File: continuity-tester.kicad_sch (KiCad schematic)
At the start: 30 parts, among them J1 Conn_01x01_Pin, J2 Conn_01x01_Pin, J3 Conn_01x01_Pin, J4 Conn_01x01_Pin, Q1 2N3906, Q2 2N3904, Q3 2N3904, U1 MCP6022

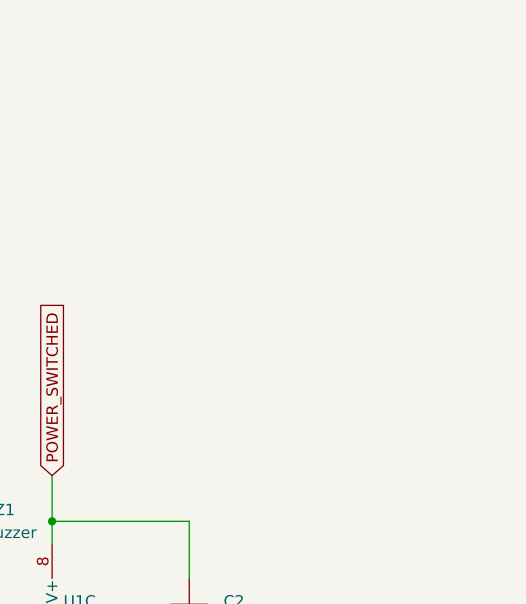
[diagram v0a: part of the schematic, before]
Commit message: added board dimensions to silkscreen
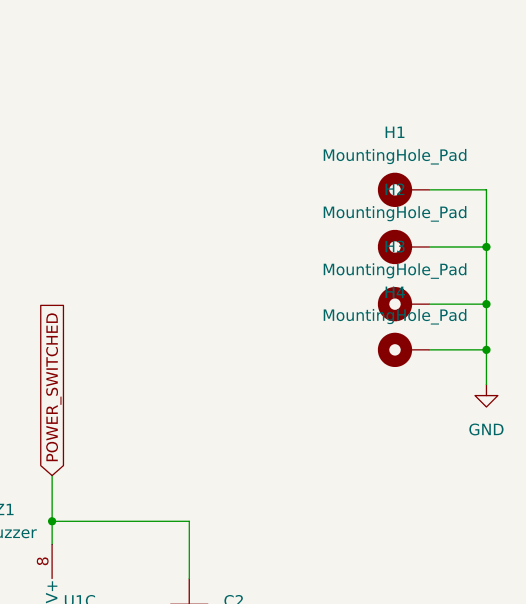
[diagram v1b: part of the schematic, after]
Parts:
- added H1, H2, H3, H4: MountingHole_Pad, MountingHole:MountingHole_2mm, symbol Mechanical:MountingHole_Pad
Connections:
- net GND: now also H1.1, H2.1, H3.1, H4.1
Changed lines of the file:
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@@
 (kicad_sch (version 20230121) (generator eeschema)
   (paper "A4")
+  (junction (at 236.22 68.58) (diameter 0) (color 0 0 0 0)
+  )
   (junction (at 92.71 101.6) (diameter 0) (color 0 0 0 0)
   )
@@
   (junction (at 129.54 96.52) (diameter 0) (color 0 0 0 0)
   )
+  (junction (at 236.22 57.15) (diameter 0) (color 0 0 0 0)
+  )
   (junction (at 127 96.52) (diameter 0) (color 0 0 0 0)
   )
   (junction (at 88.9 91.44) (diameter 0) (color 0 0 0 0)
+  )
+  (junction (at 236.22 63.5) (diameter 0) (color 0 0 0 0)
   )
   (junction (at 50.8 63.5) (diameter 0) (color 0 0 0 0)
@@
     (stroke (width 0) (type default))
   )
+  (wire (pts (xy 229.87 57.15) (xy 236.22 57.15))
+    (stroke (width 0) (type default))
+  )
   (wire (pts (xy 88.9 86.36) (xy 88.9 91.44))
     (stroke (width 0) (type default))
   )
+  (wire (pts (xy 236.22 68.58) (xy 236.22 72.39))
+    (stroke (width 0) (type default))
+  )
   (wire (pts (xy 171.45 53.34) (xy 171.45 55.88))
     (stroke (width 0) (type default))
@@
     (stroke (width 0) (type default))
   )
+  (wire (pts (xy 236.22 63.5) (xy 236.22 68.58))
+    (stroke (width 0) (type default))
+  )
   (wire (pts (xy 173.99 85.09) (xy 170.18 85.09))
     (stroke (width 0) (type default))
@@
     (stroke (width 0) (type default))
   )
+  (wire (pts (xy 236.22 50.8) (xy 236.22 57.15))
+    (stroke (width 0) (type default))
+  )
   (wire (pts (xy 88.9 91.44) (xy 88.9 92.71))
     (stroke (width 0) (type default))
   )
+  (wire (pts (xy 229.87 68.58) (xy 236.22 68.58))
+    (stroke (width 0) (type default))
+  )
   (wire (pts (xy 40.64 109.22) (xy 40.64 113.03))
     (stroke (width 0) (type default))
@@
     (stroke (width 0) (type default))
   )
+  (wire (pts (xy 236.22 57.15) (xy 236.22 63.5))
+    (stroke (width 0) (type default))
+  )
+  (wire (pts (xy 229.87 50.8) (xy 236.22 50.8))
+    (stroke (width 0) (type default))
+  )
   (wire (pts (xy 187.96 82.55) (xy 187.96 87.63))
     (stroke (width 0) (type default))
@@
   )
   (wire (pts (xy 187.96 106.68) (xy 187.96 109.22))
+    (stroke (width 0) (type default))
+  )
+  (wire (pts (xy 229.87 63.5) (xy 236.22 63.5))
     (stroke (width 0) (type default))
   )
@@
     )
   )
+  (symbol (lib_id "Mechanical:MountingHole_Pad") (at 227.33 63.5 90) (unit 1)
+    (in_bom yes) (on_board yes) (dnp no) (fields_autoplaced)
+    (property "Reference" "H3" (at 226.06 57.15 90)
+      (effects (font (size 1.27 1.27)))
+    )
+    (property "Value" "MountingHole_Pad" (at 226.06 59.69 90)
+      (effects (font (size 1.27 1.27)))
+    )
+    (property "Footprint" "MountingHole:MountingHole_2mm" (at 227.33 63.5 0)
+      (effects (font (size 1.27 1.27)) hide)
+    )
+    (property "Datasheet" "~" (at 227.33 63.5 0)
+      (effects (font (size 1.27 1.27)) hide)
+    )
+    (pin "1")
+    (instances
+      (project "continuity-tester"
+        (path "/26eed4ac-2c8e-4cb2-b316-f57caaf9169f"
+          (reference "H3") (unit 1)
+        )
+      )
+    )
+  )
   (symbol (lib_id "power:GND") (at 88.9 92.71 0) (unit 1)
     (in_bom yes) (on_board yes) (dnp no) (fields_autoplaced)
@@
         (path "/26eed4ac-2c8e-4cb2-b316-f57caaf9169f"
           (reference "R3") (unit 1)
+        )
+      )
+    )
+  )
+  (symbol (lib_id "Mechanical:MountingHole_Pad") (at 227.33 50.8 90) (unit 1)
+    (in_bom yes) (on_board yes) (dnp no) (fields_autoplaced)
+    (property "Reference" "H1" (at 226.06 44.45 90)
+      (effects (font (size 1.27 1.27)))
+    )
+    (property "Value" "MountingHole_Pad" (at 226.06 46.99 90)
+      (effects (font (size 1.27 1.27)))
+    )
+    (property "Footprint" "MountingHole:MountingHole_2mm" (at 227.33 50.8 0)
+      (effects (font (size 1.27 1.27)) hide)
+    )
+    (property "Datasheet" "~" (at 227.33 50.8 0)
+      (effects (font (size 1.27 1.27)) hide)
+    )
+    (pin "1")
+    (instances
+      (project "continuity-tester"
+        (path "/26eed4ac-2c8e-4cb2-b316-f57caaf9169f"
+          (reference "H1") (unit 1)
         )
       )
@@
     )
   )
+  (symbol (lib_id "power:GND") (at 236.22 72.39 0) (unit 1)
+    (in_bom yes) (on_board yes) (dnp no) (fields_autoplaced)
+    (property "Reference" "#PWR014" (at 236.22 78.74 0)
+      (effects (font (size 1.27 1.27)) hide)
+    )
+    (property "Value" "GND" (at 236.22 77.47 0)
+      (effects (font (size 1.27 1.27)))
+    )
+    (property "Footprint" "" (at 236.22 72.39 0)
+      (effects (font (size 1.27 1.27)) hide)
+    )
+    (property "Datasheet" "" (at 236.22 72.39 0)
+      (effects (font (size 1.27 1.27)) hide)
+    )
+    (pin "1")
+    (instances
+      (project "continuity-tester"
+        (path "/26eed4ac-2c8e-4cb2-b316-f57caaf9169f"
+          (reference "#PWR014") (unit 1)
+        )
+      )
+    )
+  )
   (symbol (lib_id "Connector:Conn_01x01_Pin") (at 33.02 101.6 0) (unit 1)
     (in_bom yes) (on_board yes) (dnp no) (fields_autoplaced)
@@
     )
   )
+  (symbol (lib_id "Mechanical:MountingHole_Pad") (at 227.33 57.15 90) (unit 1)
+    (in_bom yes) (on_board yes) (dnp no) (fields_autoplaced)
+    (property "Reference" "H2" (at 226.06 50.8 90)
+      (effects (font (size 1.27 1.27)))
+    )
+    (property "Value" "MountingHole_Pad" (at 226.06 53.34 90)
+      (effects (font (size 1.27 1.27)))
+    )
+    (property "Footprint" "MountingHole:MountingHole_2mm" (at 227.33 57.15 0)
+      (effects (font (size 1.27 1.27)) hide)
+    )
+    (property "Datasheet" "~" (at 227.33 57.15 0)
+      (effects (font (size 1.27 1.27)) hide)
+    )
+    (pin "1")
+    (instances
+      (project "continuity-tester"
+        (path "/26eed4ac-2c8e-4cb2-b316-f57caaf9169f"
+          (reference "H2") (unit 1)
+        )
+      )
+    )
+  )
   (symbol (lib_id "power:GND") (at 40.64 113.03 0) (unit 1)
     (in_bom yes) (on_board yes) (dnp no) (fields_autoplaced)
@@
         )
       )
+    )
+  )
+  (symbol (lib_id "Mechanical:MountingHole_Pad") (at 227.33 68.58 90) (unit 1)
+    (in_bom yes) (on_board yes) (dnp no) (fields_autoplaced)
+    (property "Reference" "H4" (at 226.06 62.23 90)
+      (effects (font (size 1.27 1.27)))
+    )
+    (property "Value" "MountingHole_Pad" (at 226.06 64.77 90)
+      (effects (font (size 1.27 1.27)))
+    )
+    (property "Footprint" "MountingHole:MountingHole_2mm" (at 227.33 68.58 0)
+      (effects (font (size 1.27 1.27)) hide)
+    )
+    (property "Datasheet" "~" (at 227.33 68.58 0)
+      (effects (font (size 1.27 1.27)) hide)
+    )
+    (pin "1")
+    (instances
+      (project "continuity-tester"
+        (path "/26eed4ac-2c8e-4cb2-b316-f57caaf9169f"
+          (reference "H4") (unit 1)
+        )
+      )
